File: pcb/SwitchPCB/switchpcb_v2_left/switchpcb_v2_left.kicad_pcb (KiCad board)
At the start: 2 copper layers, 187 x 27 mm, 64 parts, among them J1 Conn_01x08, Q10 2N7002, Q11 BC847, Q12 2N7002, Q13 BC847, Q14 2N7002, Q15 BC847, Q16 2N7002, Q17 BC847, Q18 BC847, Q19 2N7002, Q20 2N7002, Q21 BC847, Q22 BC847, Q23 2N7002, Q24 2N7002, Q5 BC847, Q6 2N7002, Q7 BC847, Q8 2N7002, Q9 BC847, SW2 Lehle_Switch, SW3 Lehle_Switch, SW4 Lehle_Switch, U1 74HC595, U2 74HC595

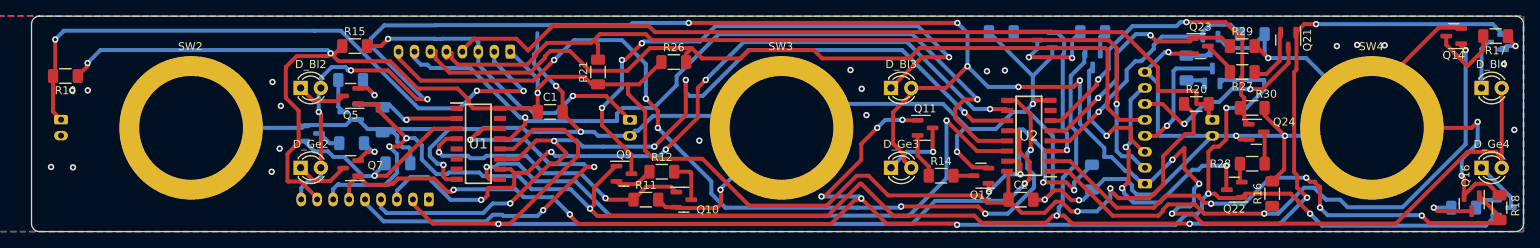
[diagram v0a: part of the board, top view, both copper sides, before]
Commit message: New switch pcb version with IO expander
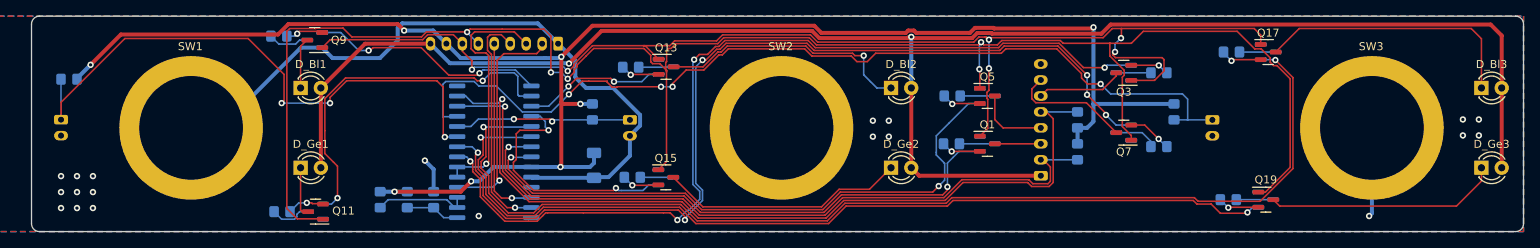
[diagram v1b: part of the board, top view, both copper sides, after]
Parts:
- removed C2: 100n, Capacitor_SMD:C_1206_3216Metric_Pad1.33x1.80mm_HandSolder
- removed J_Main2: Conn_01x08, Connector_JST:JST_PH_B8B-PH-K_1x08_P2.00mm_Vertical
- removed the R13 at (317.9, 93.2)
- removed the R16 at (340.5, 95.2)
- removed the R18 at (369.0, 97.0)
- removed R24, R25, R29, R30: 100k, Resistor_SMD:R_1206_3216Metric_Pad1.30x1.75mm_HandSolder
- removed the R6 at (229.0, 86.0)
- removed the R8 at (230.9, 91.5)
- removed U2: 74HC595, SamacSys_Parts:SOIC127P600X175-16N
- added R10: 10k, Resistor_SMD:R_0805_2012Metric_Pad1.20x1.40mm_HandSolder, B.Cu at (228.7, 96.0)
- added R12: 10k, Resistor_SMD:R_0805_2012Metric_Pad1.20x1.40mm_HandSolder, B.Cu at (235.4, 96.0)
- C1: moved to B.Cu
- Q1: renamed from Q17; moved to F.Cu
- Q14: renamed from Q10; moved to B.Cu
- Q16: renamed from Q12; moved to B.Cu
- Q17: renamed from Q13; moved to F.Cu
- Q18: renamed from Q14; moved to B.Cu
- Q19: renamed from Q15; moved to F.Cu
- Q20: renamed from Q16; moved to B.Cu
- Q4: renamed from Q23; moved to B.Cu
- Q5: renamed from Q18; moved to F.Cu
- Q8: renamed from Q24; moved to B.Cu
- R1: renamed from R26; footprint Resistor_SMD:R_1206_3216Metric_Pad1.30x1.75mm_HandSolder -> Resistor_SMD:R_0805_2012Metric_Pad1.20x1.40mm_HandSolder; moved to B.Cu
- R11: value 100k -> 10k; footprint Resistor_SMD:R_1206_3216Metric_Pad1.30x1.75mm_HandSolder -> Resistor_SMD:R_0805_2012Metric_Pad1.20x1.40mm_HandSolder; moved to B.Cu
- R13: renamed from R12; footprint Resistor_SMD:R_1206_3216Metric_Pad1.30x1.75mm_HandSolder -> Resistor_SMD:R_0805_2012Metric_Pad1.20x1.40mm_HandSolder; moved to B.Cu
- R14, R15: footprint Resistor_SMD:R_1206_3216Metric_Pad1.30x1.75mm_HandSolder -> Resistor_SMD:R_0805_2012Metric_Pad1.20x1.40mm_HandSolder; moved to B.Cu
- R16: renamed from R17; footprint Resistor_SMD:R_1206_3216Metric_Pad1.30x1.75mm_HandSolder -> Resistor_SMD:R_0805_2012Metric_Pad1.20x1.40mm_HandSolder; moved to B.Cu
- R17: renamed from R19; footprint Resistor_SMD:R_1206_3216Metric_Pad1.30x1.75mm_HandSolder -> Resistor_SMD:R_0805_2012Metric_Pad1.20x1.40mm_HandSolder
- R18: renamed from R20; footprint Resistor_SMD:R_1206_3216Metric_Pad1.30x1.75mm_HandSolder -> Resistor_SMD:R_0805_2012Metric_Pad1.20x1.40mm_HandSolder; moved to B.Cu
- R2: renamed from R21; footprint Resistor_SMD:R_1206_3216Metric_Pad1.30x1.75mm_HandSolder -> Resistor_SMD:R_0805_2012Metric_Pad1.20x1.40mm_HandSolder; moved to B.Cu
- R3: renamed from R22; footprint Resistor_SMD:R_1206_3216Metric_Pad1.30x1.75mm_HandSolder -> Resistor_SMD:R_0805_2012Metric_Pad1.20x1.40mm_HandSolder
- R4: renamed from R27; footprint Resistor_SMD:R_1206_3216Metric_Pad1.30x1.75mm_HandSolder -> Resistor_SMD:R_0805_2012Metric_Pad1.20x1.40mm_HandSolder; moved to B.Cu
- R5: renamed from R23; footprint Resistor_SMD:R_1206_3216Metric_Pad1.30x1.75mm_HandSolder -> Resistor_SMD:R_0805_2012Metric_Pad1.20x1.40mm_HandSolder
- R6: renamed from R28; footprint Resistor_SMD:R_1206_3216Metric_Pad1.30x1.75mm_HandSolder -> Resistor_SMD:R_0805_2012Metric_Pad1.20x1.40mm_HandSolder; moved to B.Cu
- R7: footprint Resistor_SMD:R_1206_3216Metric_Pad1.30x1.75mm_HandSolder -> Resistor_SMD:R_0805_2012Metric_Pad1.20x1.40mm_HandSolder
- R8: renamed from R9; footprint Resistor_SMD:R_1206_3216Metric_Pad1.30x1.75mm_HandSolder -> Resistor_SMD:R_0805_2012Metric_Pad1.20x1.40mm_HandSolder
- R9: renamed from R10; footprint Resistor_SMD:R_1206_3216Metric_Pad1.30x1.75mm_HandSolder -> Resistor_SMD:R_0805_2012Metric_Pad1.20x1.40mm_HandSolder; moved to B.Cu
- U1: value 74HC595 -> MCP23017_SO; footprint SamacSys_Parts:SOIC127P600X175-16N -> Package_SO:SOIC-28W_7.5x17.9mm_P1.27mm; moved to B.Cu
- moved R2 60.9 mm to (316.1, 90.0), turned to -90 degrees
- moved R1 51.1 mm to (316.1, 86.0), turned to 90 degrees
- moved Q16 39.5 mm to (264.5, 93.2), turned to 0 degrees
- moved R14 38.7 mm to (260.3, 93.2)
- moved R16 33.2 mm to (335.4, 77.5), turned to 0 degrees
- moved Q15 33.1 mm to (264.5, 93.2)
- moved R15 30.9 mm to (255.3, 85.0), turned to -90 degrees
- moved R11 29.9 mm to (232.1, 96.0), turned to -90 degrees
- moved Q19 29.8 mm to (339.7, 96.0)
- moved R5 29.6 mm to (300.4, 83.0), turned to 0 degrees
- moved R17 29.5 mm to (335.0, 96.0), turned to 0 degrees
- moved Q6 28.7 mm to (304.8, 83.0), turned to 0 degrees
- moved Q17 28.5 mm to (340.0, 77.5), turned to 0 degrees
- moved Q5 28.3 mm to (304.8, 83.0), turned to 0 degrees
- moved Q20 25.8 mm to (339.7, 96.0), turned to 0 degrees
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- renumbered D_Bl2 to D_Bl1, D_Bl3 to D_Bl2, D_Bl4 to D_Bl3, D_Ge2 to D_Ge1, D_Ge3 to D_Ge2, D_Ge4 to D_Ge3, J_SW2 to J_SW1, J_SW3 to J_SW2, J_SW4 to J_SW3, Q6 to Q10, Q7 to Q11, Q8 to Q12, Q9 to Q13, Q11 to Q15, Q19 to Q2, Q21 to Q3, Q20 to Q6, Q22 to Q7, Q5 to Q9, SW2 to SW1, SW3 to SW2, SW4 to SW3
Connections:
- J_Main1 pad 2: /RCLK -> /RESET_N
- J_Main1 pad 3: /SRCLR -> /INT
- J_Main1 pad 4: /SRCLK -> /SDA
- J_Main1 pad 5: /SER -> /SCK
- R11 pad 1: /On_3 -> /VDD3V3
- R11 pad 2: GND -> Net-(R12-Pad1)
- U1 pad 1: /Stomp_1 -> /On_2
- U1 pad 10: /SRCLR -> GND
- U1 pad 11: /SRCLK -> unconnected-(U1-Pad11)
- U1 pad 12: /RCLK -> /SCK
- U1 pad 13: /OE -> /SDA
- U1 pad 14: /SER -> unconnected-(U1-Pad14)
- U1 pad 15: /On_1 -> Net-(R12-Pad1)
- U1 pad 16: /VDD3V3 -> Net-(R10-Pad2)
- U1 pad 2: /On_2 -> /Stomp_2
- U1 pad 3: /Stomp_2 -> /On_3
- U1 pad 4: /On_3 -> /Stomp_3
- U1 pad 5: unconnected-(U1-Pad5) -> /On_4
- U1 pad 6: unconnected-(U1-Pad6) -> /Stomp_4
- U1 pad 7: unconnected-(U1-Pad7) -> /On_5
- U1 pad 8: GND -> /Stomp_5
- U1 pad 9: Net-(U1-Pad9) -> /VDD3V3
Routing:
- net GND: track 356.8 -> 100.6 mm, vias 33 -> 20
- net /RCLK: track 115.1 -> 0.00 mm, vias 2 -> 0
- net /SER_OUT: track 112.3 -> 0.00 mm, vias 6 -> 0
- net /SRCLK: track 108.6 -> 0.00 mm, vias 5 -> 0
- net /OE: track 100.8 -> 0.00 mm, vias 2 -> 0
- net /SRCLR: track 97.2 -> 0.00 mm, vias 5 -> 0
- net /On_6: track 30.4 -> 113.2 mm, vias 2 -> 4
- net Net-(U1-Pad9): track 81.9 -> 0.00 mm, vias 2 -> 0
- net /Stomp_6: track 42.9 -> 119.0 mm, vias 2 -> 6
- net /Vref_blue: track 226.4 -> 158.6 mm, vias 7 -> 6
- net /On_4: track 75.4 -> 137.5 mm
- net /SER: track 56.9 -> 0.00 mm, vias 3 -> 0
- net /On_5: track 22.9 -> 72.7 mm, vias 1 -> 2
- net /Stomp_4: track 68.9 -> 115.5 mm, vias 4 -> 2
- net /Stomp_5: track 31.9 -> 75.6 mm, vias 1 -> 2
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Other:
- board text added: "Addr. 6"
- board text added: "Addr. 7"
- board text added: "Controller Switch Left Rev. 2.0"
- board text removed: "Controller Switch Left Rev. 1.0"
